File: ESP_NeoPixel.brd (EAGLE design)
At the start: 160 x 100 mm, 0 parts

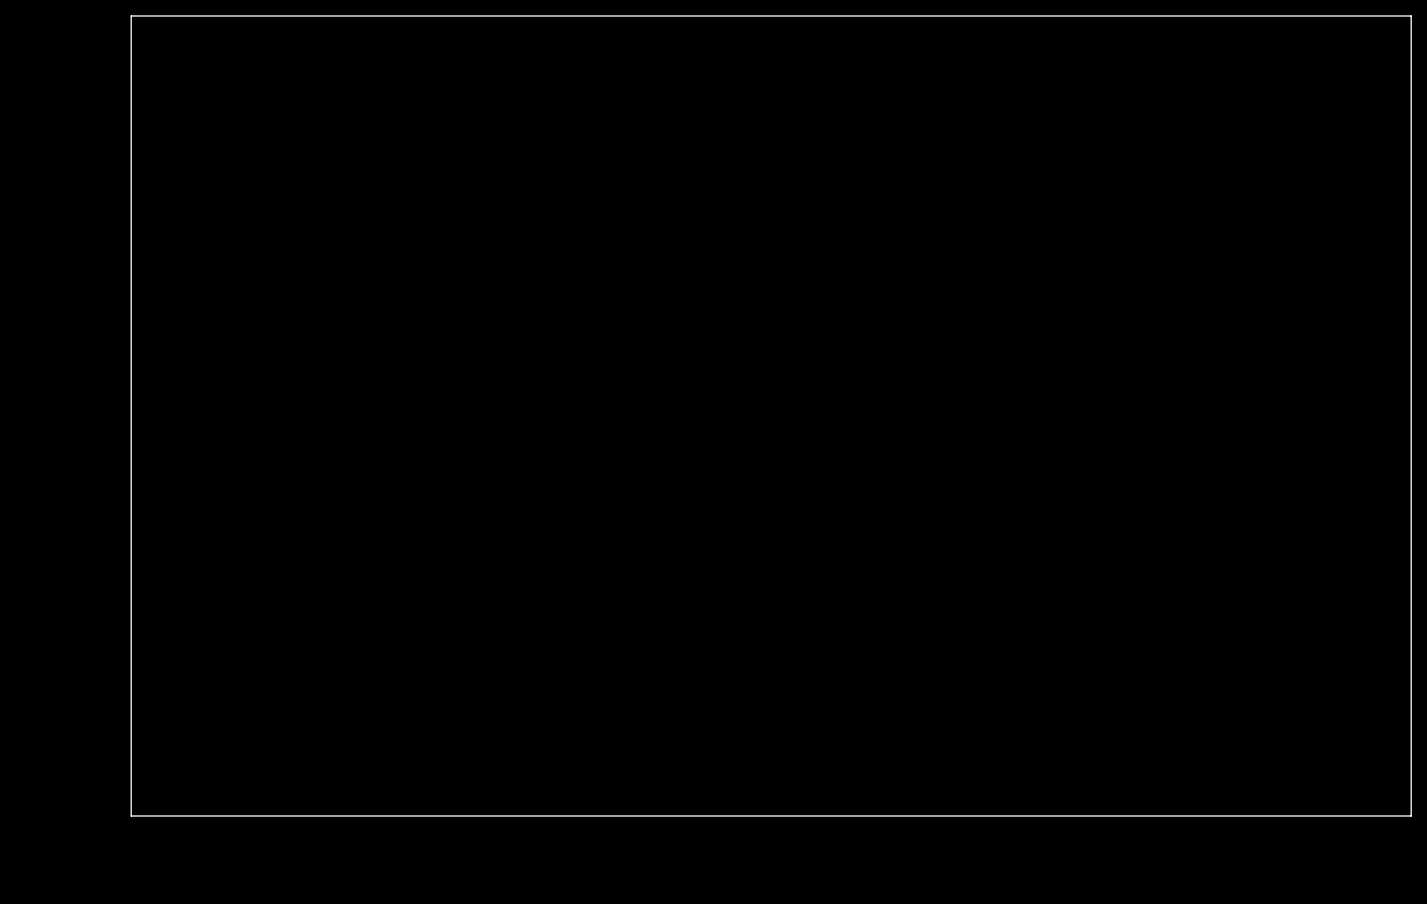
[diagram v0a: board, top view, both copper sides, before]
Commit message: dimensions and wemos pins
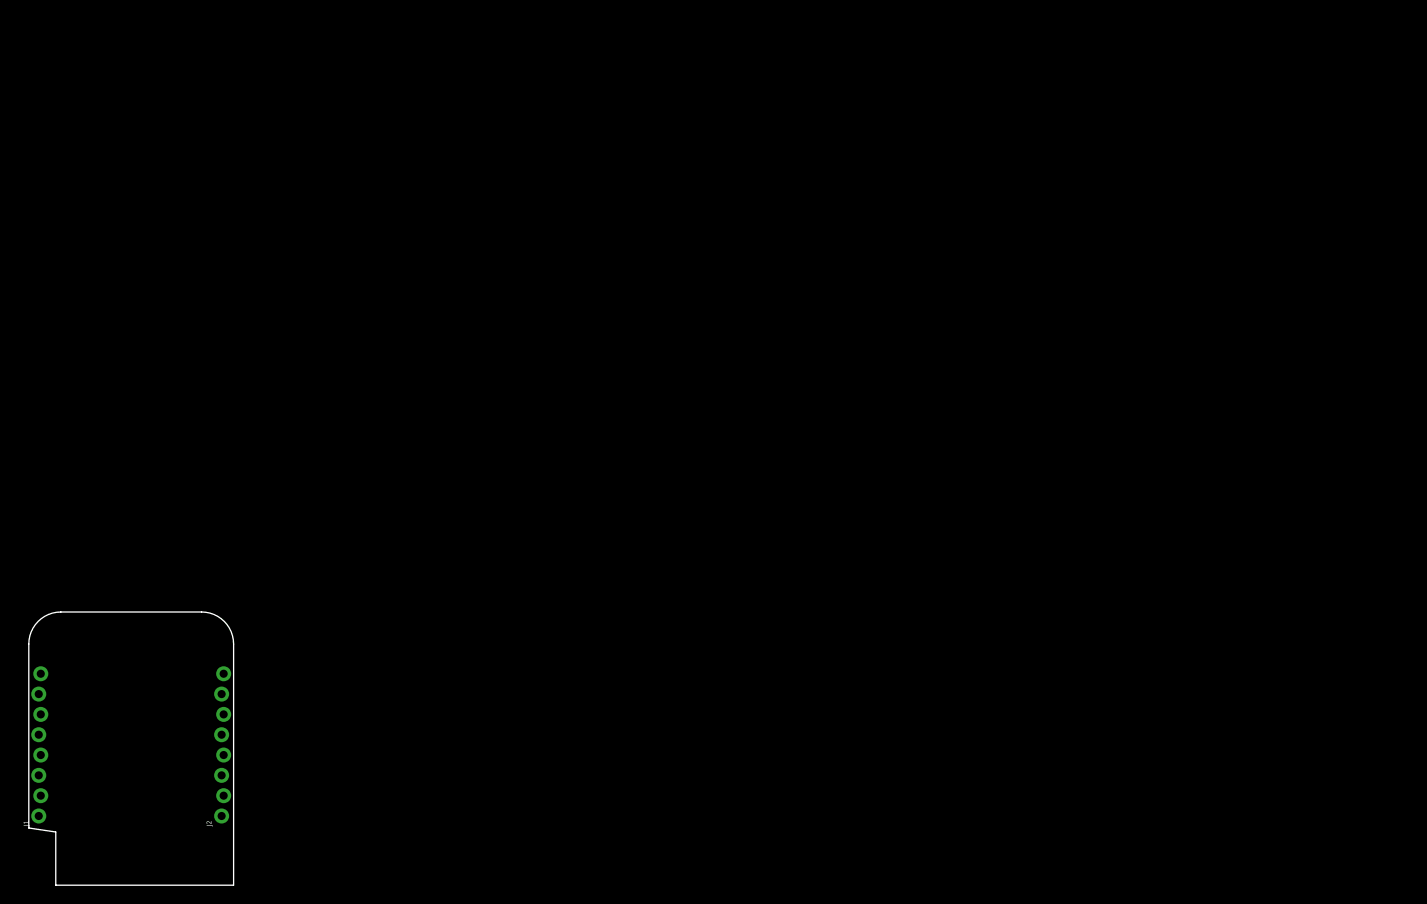
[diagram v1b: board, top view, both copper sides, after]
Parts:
- added J1, J2: (no value), SparkFun-Connectors:1X08_LOCK_NO_SILK
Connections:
- new net +3V3: J1.1
- new net +5V: J2.1
- new net A0: J1.7
- new net D0: J1.6
- new net D1: J2.6
- new net D2: J2.5
- new net D3: J2.4
- new net D4: J2.3
- new net D5: J1.5
- new net D6: J1.4
- new net D7: J1.3
- new net D8: J1.2
- new net GND: J2.2
- new net RST: J1.8
- new net RX: J2.7
- new net TX: J2.8
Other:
- board size 160 x 100 mm -> 25.6 x 34.1 mm

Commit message: did the thing
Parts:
- added C1, C3: 10µF, rcl:C0805
- added C2: 1nF, rcl:C0603
- added J3: MKDS3-2-5.00, jonas-phoenix:MKDS3-2-5.00
- added J4: MKDS3-3-5.00, jonas-phoenix:MKDS3-3-5.00
- added JP1: JUMPER-SMT_2_NO_SILK, SparkFun-Jumpers:SMT-JUMPER_2_NO_SILK
- added LOGO1: OSHW-LOGOS, SparkFun-Aesthetics:OSHW-LOGO-S
- added Q1: BSN20,215, jonas_mosfet:BSN20_215
- added R1: 14.7k, rcl:R0603
- added R2: 2.8k, rcl:R0603
- added R3, R4: 4.7k, rcl:R0603
- added U1: LMZ21700, jonas_ti:SIL0008E
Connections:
- removed net D5: J1.5
- new net N$1: R1.1, R2.2, U1.P2
- new net N$2: C2.1, U1.P1
- new net NEOPIX_3V3: J1.5, Q1.2, R3.1
- new net NEOPIX_5V: J4.2, Q1.3, R4.1
- new net VCC: C1.1, J3.1, J4.1, JP1.1, U1.P7, U1.P8
- net +3V3: now also Q1.1, R3.2
- net +5V: now also C3.1, JP1.2, R1.2, R4.2, U1.P4, U1.P6
- net GND: now also C1.2, C2.2, C3.2, J3.2, J4.3, R2.1, U1.P10, U1.P5, U1.P9
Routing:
- net VCC: track 0.00 -> 42.4 mm
- net +5V: track 0.00 -> 37.4 mm, vias 0 -> 4
- net NEOPIX_5V: track 0.00 -> 14.0 mm
- net +3V3: track 0.00 -> 13.3 mm
- net NEOPIX_3V3: track 0.00 -> 9.56 mm
- net N$1: track 0.00 -> 3.49 mm
- net GND: track 0.00 -> 2.80 mm, vias 0 -> 24
- net N$2: track 0.00 -> 2.00 mm
- added copper zone on layer 1, net +5V
- added copper zone on layer 1, net GND
- added copper zone on layer 16, net GND
- added copper zone on layer 1, net VCC
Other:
- board text added: "+ S -"
- board text added: "+-"
- board text added: "+S-"
- board text added: "5-17V"
- board text added: "github.com /ottojo /amg8833"

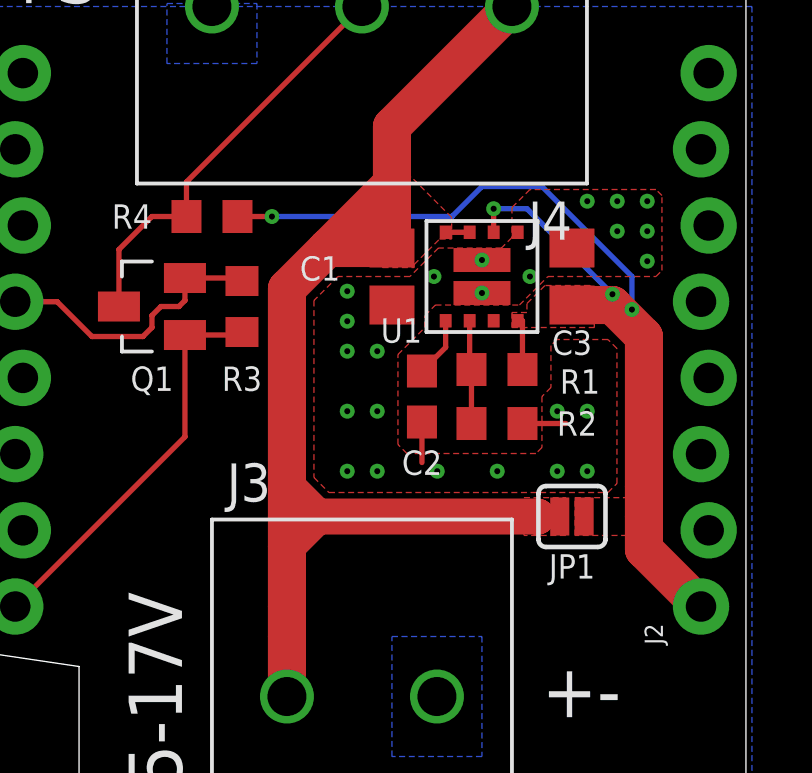
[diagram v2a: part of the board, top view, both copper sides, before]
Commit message: values, silkscreen
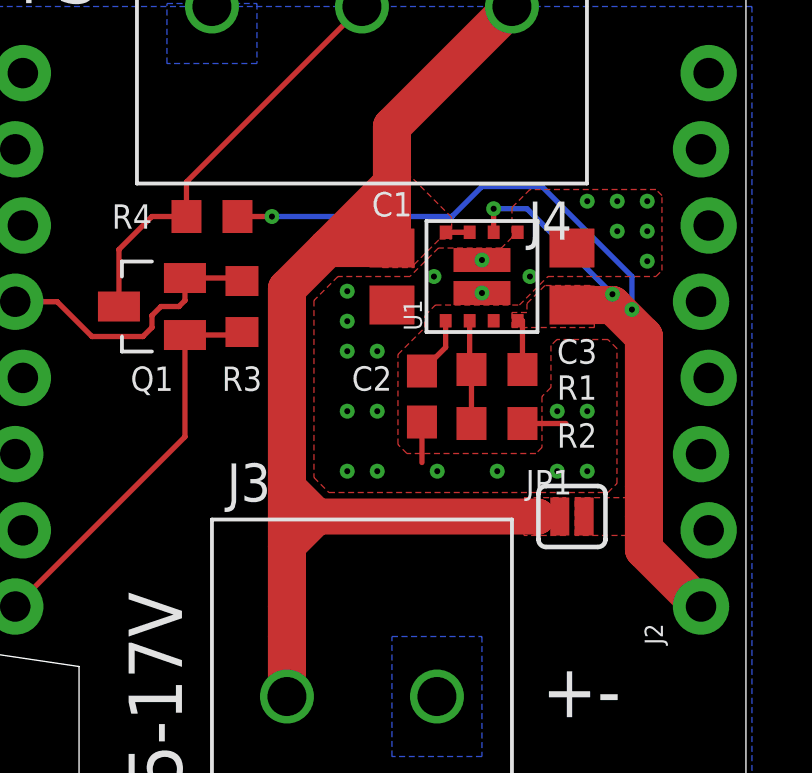
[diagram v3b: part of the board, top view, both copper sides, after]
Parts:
- C1, C3: value 10µF -> 22µF

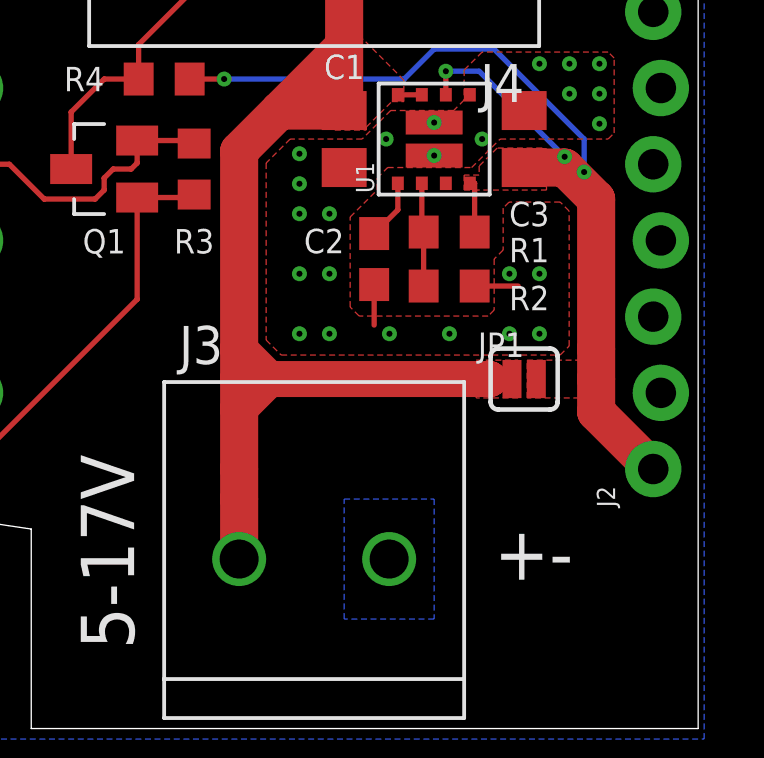
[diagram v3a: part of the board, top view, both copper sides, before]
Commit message: silkscreen, gnd connection to esp
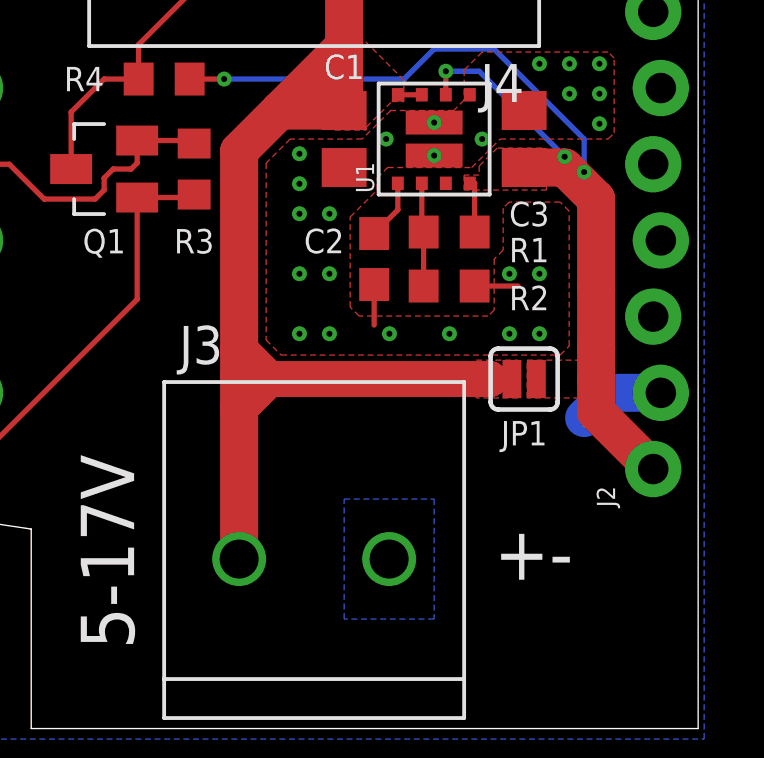
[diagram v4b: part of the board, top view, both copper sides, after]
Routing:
- net GND: track 2.80 -> 5.70 mm
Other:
- board text added: "github.com /ottojo /wifiblink"
- board text removed: "github.com /ottojo /amg8833"
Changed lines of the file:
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@@
 <layer number="14" name="Route14" color="22" fill="1" visible="no" active="no"/>
 <layer number="15" name="Route15" color="23" fill="1" visible="no" active="no"/>
-<layer number="16" name="Bottom" color="1" fill="1" visible="no" active="yes"/>
+<layer number="16" name="Bottom" color="1" fill="1" visible="yes" active="yes"/>
 <layer number="17" name="Pads" color="2" fill="1" visible="yes" active="yes"/>
 <layer number="18" name="Vias" color="2" fill="1" visible="yes" active="yes"/>
@@
 <layer number="20" name="Dimension" color="24" fill="1" visible="yes" active="yes"/>
 <layer number="21" name="tPlace" color="7" fill="1" visible="yes" active="yes"/>
-<layer number="22" name="bPlace" color="7" fill="1" visible="no" active="yes"/>
+<layer number="22" name="bPlace" color="7" fill="1" visible="yes" active="yes"/>
 <layer number="23" name="tOrigins" color="15" fill="1" visible="yes" active="yes"/>
-<layer number="24" name="bOrigins" color="15" fill="1" visible="no" active="yes"/>
+<layer number="24" name="bOrigins" color="15" fill="1" visible="yes" active="yes"/>
 <layer number="25" name="tNames" color="7" fill="1" visible="yes" active="yes"/>
-<layer number="26" name="bNames" color="7" fill="1" visible="no" active="yes"/>
+<layer number="26" name="bNames" color="7" fill="1" visible="yes" active="yes"/>
 <layer number="27" name="tValues" color="7" fill="1" visible="no" active="yes"/>
 <layer number="28" name="bValues" color="7" fill="1" visible="no" active="yes"/>
@@
 <layer number="38" name="bTest" color="7" fill="1" visible="no" active="yes"/>
 <layer number="39" name="tKeepout" color="4" fill="11" visible="yes" active="yes"/>
-<layer number="40" name="bKeepout" color="1" fill="11" visible="no" active="yes"/>
+<layer number="40" name="bKeepout" color="1" fill="11" visible="yes" active="yes"/>
 <layer number="41" name="tRestrict" color="4" fill="10" visible="yes" active="yes"/>
-<layer number="42" name="bRestrict" color="1" fill="10" visible="no" active="yes"/>
+<layer number="42" name="bRestrict" color="1" fill="10" visible="yes" active="yes"/>
 <layer number="43" name="vRestrict" color="2" fill="10" visible="no" active="yes"/>
 <layer number="44" name="Drills" color="7" fill="1" visible="no" active="yes"/>
@@
 <layer number="50" name="dxf" color="7" fill="1" visible="no" active="no"/>
 <layer number="51" name="tDocu" color="7" fill="1" visible="yes" active="yes"/>
-<layer number="52" name="bDocu" color="7" fill="1" visible="no" active="yes"/>
+<layer number="52" name="bDocu" color="7" fill="1" visible="yes" active="yes"/>
 <layer number="53" name="tGND_GNDA" color="7" fill="9" visible="no" active="no"/>
 <layer number="54" name="bGND_GNDA" color="1" fill="9" visible="no" active="no"/>
@@
 <text x="2" y="11" size="1.778" layer="22" ratio="12" rot="MR90" align="bottom-right">github.com
 /ottojo
-/amg8833</text>
+/wifiblink</text>
 </plain>
 <attributes>
@@
 </element>
 <element name="JP1" library="SparkFun-Jumpers" library_urn="urn:adsk.eagle:library:528" package="SMT-JUMPER_2_NO_SILK" package3d_urn="urn:adsk.eagle:package:39279/1" value="JUMPER-SMT_2_NO_SILK" x="7" y="3">
-<attribute name="NAME" x="7" y="4.143" size="0.8128" layer="25" font="vector" align="center-right"/>
+<attribute name="NAME" x="7" y="1.6" size="0.8128" layer="25" font="vector" align="top-center"/>
 <attribute name="VALUE" x="7" y="1.857" size="0.6096" layer="27" font="vector" ratio="20" align="top-center"/>
 </element>
@@
 <wire x1="8.35" y1="10.05" x2="9.4" y2="9" width="1.27" layer="1"/>
 <wire x1="9.4" y1="1.903" x2="11.303" y2="0" width="1.27" layer="1"/>
-<wire x1="9.4" y1="9" x2="9.4" y2="4" width="1.27" layer="1"/>
+<wire x1="9.4" y1="9" x2="9.4" y2="6" width="1.27" layer="1"/>
+<wire x1="9.4" y1="6" x2="9.4" y2="4" width="1.27" layer="1"/>
 <wire x1="9.4" y1="4" x2="9.4" y2="3" width="1.27" layer="1"/>
 <wire x1="9.4" y1="3" x2="9.4" y2="1.903" width="1.27" layer="1"/>
@@
 <via x="7.51" y="6.51" extent="1-16" drill="0.2"/>
 <via x="6.51" y="6.51" extent="1-16" drill="0.2"/>
+<wire x1="11.557" y1="2.54" x2="9.84" y2="2.54" width="1.27" layer="16"/>
+<wire x1="9.84" y1="2.54" x2="9" y2="1.7" width="1.27" layer="16"/>
 </signal>
 <signal name="+3V3">
@@
 <contactref element="U1" pad="P7"/>
 <contactref element="C1" pad="1"/>
-<wire x1="-2.5" y1="-3" x2="-2.5" y2="-1" width="1.27" layer="1"/>
-<wire x1="-2.5" y1="-1" x2="-2.5" y2="0" width="1.27" layer="1"/>
-<wire x1="-2.5" y1="0" x2="-2.5" y2="2" width="1.27" layer="1"/>
+<wire x1="-2.5" y1="-3" x2="-2.5" y2="2" width="1.27" layer="1"/>
 <wire x1="-2.5" y1="2" x2="-2.5" y2="3" width="1.27" layer="1"/>
 <wire x1="-2.5" y1="3" x2="-2.5" y2="4" width="1.27" layer="1"/>
@@
 <mfgpreviewcolor name="soldermaskcolor" color="0xC8008000"/>
 <mfgpreviewcolor name="silkscreencolor" color="0xFFFEFEFE"/>
-<mfgpreviewcolor name="backgroundcolor" color="0xFF282828"/>
+<mfgpreviewcolor name="backgroundcolor" color="0x282828"/>
 <mfgpreviewcolor name="coppercolor" color="0xFFFFBF00"/>
 <mfgpreviewcolor name="substratecolor" color="0xFF786E46"/>
